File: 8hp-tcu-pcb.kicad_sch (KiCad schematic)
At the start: 0 parts

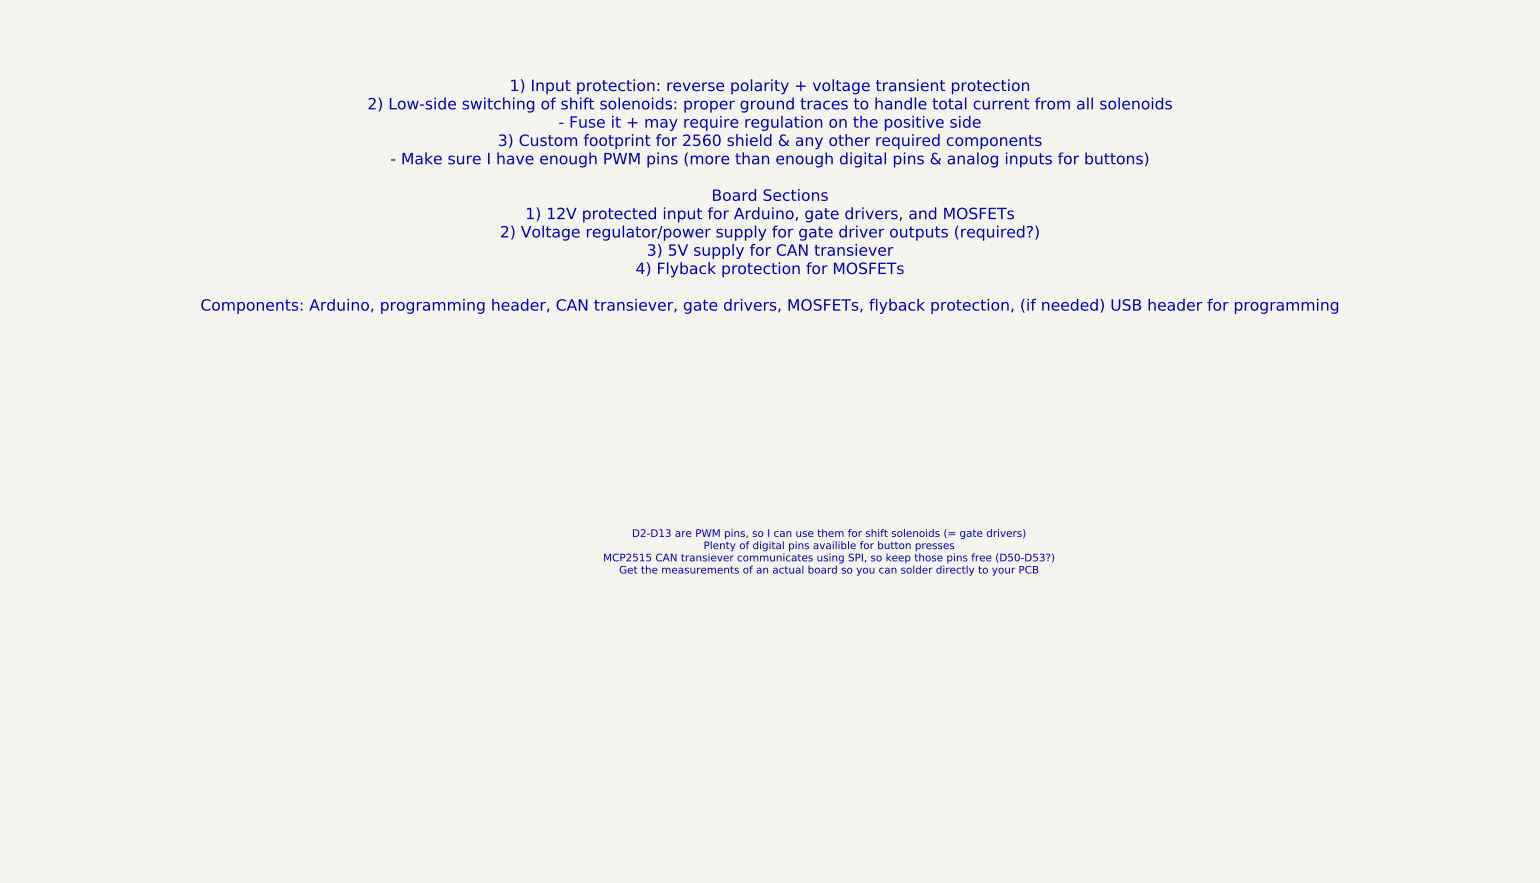
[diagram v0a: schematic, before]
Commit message: Updating several files, made a schematic for internal transmission PCB
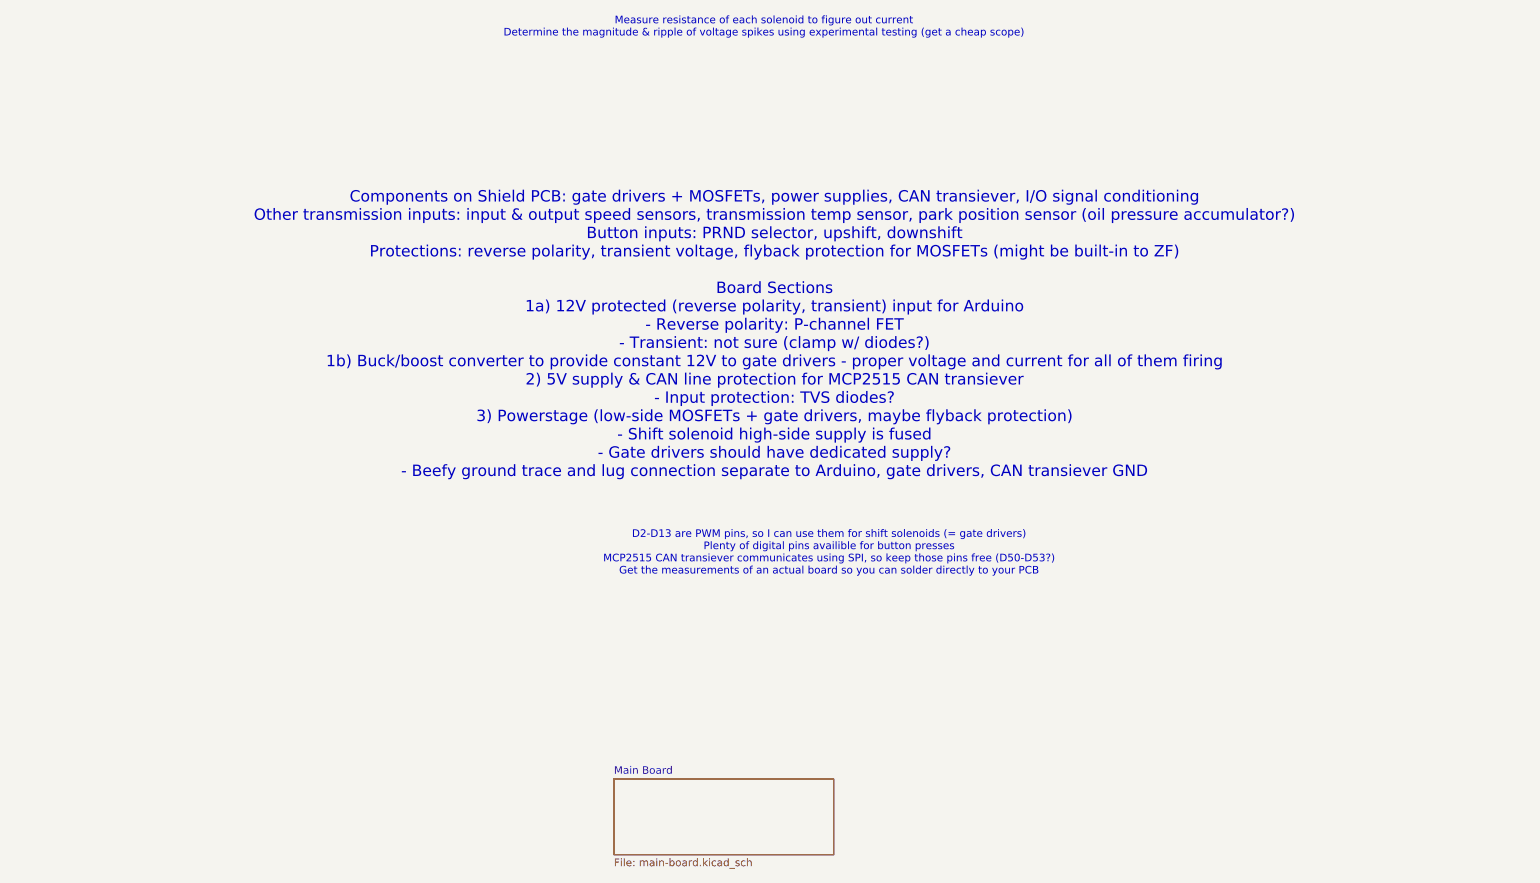
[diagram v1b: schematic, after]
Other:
- added sheet Main Board (main-board.kicad_sch)
- note added: "Components on Shield PCB: gate drivers + MOSFETs, power supplies, CAN transiever, I/O signal conditioning Other transmission inputs: input & output speed sensors, transmission temp sensor, park position sensor (oil pressure accumulator?) Button inputs: PRND selector, upshift, downshift Protections: reverse polarity, transient voltage, flyback protection for MOSFETs (might be built-in to ZF) Board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"
- note added: "Measure resistance of each solenoid to figure out current Determine the magnitude & ripple of voltage spikes using experimental testing (get a cheap scope)"
- note removed: "1) Input protection: reverse polarity + voltage transient protection 2) Low-side switching of shift solenoids: proper ground traces to handle total current from all solenoids - Fuse it + may require regulation on the positive side 3) Custom footprint for 2560 shield & any other required components - Make sure I have enough PWM pins (more than enough digital pins & analog inputs for buttons) Board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"
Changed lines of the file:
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@@
 		(company "Joelathan Racing")
+	)
+	(text "Measure resistance of each solenoid to figure out current\nDetermine the magnitude & ripple of voltage spikes using experimental testing (get a cheap scope)\n"
+		(exclude_from_sim no)
+		(at 125.476 46.736 0)
+		(effects
+			(font
+				(size 1.27 1.27)
+			)
+		)
 	)
 	(text "D2-D13 are PWM pins, so I can use them for shift solenoids (= gate drivers)\nPlenty of digital pins availible for button presses\nMCP2515 CAN transiever communicates using SPI, so keep those pins free (D50-D53?)\nGet the measurements of an actual board so you can solder directly to your PCB"
@@
 		)
 	)
-	(text "1) Input protection: reverse polarity + voltage transient protection\n2) Low-side switching of shift solenoids: proper ground traces to handle total current from all solenoids\n- Fuse it + may require regulation on the positive side\n3) Custom footprint for 2560 shield & any other required components\n- Make sure I have enough PWM pins (more than enough digital pins & analog inputs for buttons)\n\nBoard Sections\n1) 12V protected input for Arduino, gate drivers, and MOSFETs\n2) Voltage regulator/power supply for gate driver outputs (required?)\n3) 5V supply for CAN transiever \n4) Flyback protection for MOSFETs\n\nComponents: Arduino, programming header, CAN transiever, gate drivers, MOSFETs, flyback protection, (if needed) USB header for programming"
+	(text "Components on Shield PCB: gate drivers + MOSFETs, power supplies, CAN transiever, I/O signal conditioning\nOther transmission inputs: input & output speed sensors, transmission temp sensor, park position sensor (oil pressure accumulator?)\nButton inputs: PRND selector, upshift, downshift\nProtections: reverse polarity, transient voltage, flyback protection for MOSFETs (might be built-in to ZF)\n\nBoard Sections\n1a) 12V protected (reverse polarity, transient) input for Arduino\n- Reverse polarity: P-channel FET\n- Transient: not sure (clamp w/ diodes?)\n1b) Buck/boost converter to provide constant 12V to gate drivers - proper voltage and current for all of them firing\n2) 5V supply & CAN line protection for MCP2515 CAN transiever\n- Input protection: TVS diodes?\n3) Powerstage (low-side MOSFETs + gate drivers, maybe flyback protection)\n- Shift solenoid high-side supply is fused\n- Gate drivers should have dedicated supply?\n- Beefy ground trace and lug connection separate to Arduino, gate drivers, CAN transiever GND"
 		(exclude_from_sim no)
-		(at 126.492 75.184 0)
+		(at 127.254 98.298 0)
 		(effects
 			(font
@@
 			)
 		)
+	)
+	(sheet
+		(at 100.33 172.72)
+		(size 36.83 12.7)
+		(fields_autoplaced yes)
+		(stroke
+			(width 0.1524)
+			(type solid)
+		)
+		(fill
+			(color 0 0 0 0.0000)
+		)
+		(property "Sheetname" "Main Board"
+			(at 100.33 172.0084 0)
+			(effects
+				(font
+					(size 1.27 1.27)
+				)
+				(justify left bottom)
+			)
+		)
+		(property "Sheetfile" "main-board.kicad_sch"
+			(at 100.33 186.0046 0)
+			(effects
+				(font
+					(size 1.27 1.27)
+				)
+				(justify left top)
+			)
+		)
+		(instances
+			(project "8hp-tcu-pcb"
+				(path "/fab55a76-018d-479e-806d-47398c1ea91a"
+					(page "2")
+				)
+			)
+		)

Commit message: Repo update
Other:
- sheet Main Board renamed Power Stage
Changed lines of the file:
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@@
 		)
 	)
-	(text "Components on Shield PCB: gate drivers + MOSFETs, power supplies, CAN transiever, I/O signal conditioning\nOther transmission inputs: input & output speed sensors, transmission temp sensor, park position sensor (oil pressure accumulator?)\nButton inputs: PRND selector, upshift, downshift\nProtections: reverse polarity, transient voltage, flyback protection for MOSFETs (might be built-in to ZF)\n\nBoard Sections\n1a) 12V protected (reverse polarity, transient) input for Arduino\n- Reverse polarity: P-channel FET\n- Transient: not sure (clamp w/ diodes?)\n1b) Buck/boost converter to provide constant 12V to gate drivers - proper voltage and current for all of them firing\n2) 5V supply & CAN line protection for MCP2515 CAN transiever\n- Input protection: TVS diodes?\n3) Powerstage (low-side MOSFETs + gate drivers, maybe flyback protection)\n- Shift solenoid high-side supply is fused\n- Gate drivers should have dedicated supply?\n- Beefy ground trace and lug connection separate to Arduino, gate drivers, CAN transiever GND"
+	(text "Components on Shield PCB: gate drivers + MOSFETs, power supplies, CAN transiever, I/O signal conditioning\nOther transmission inputs: input & output speed sensors, transmission temp sensor, park position sensor (oil pressure accumulator?)\nButton inputs: PRND selector, upshift, downshift\nProtections: reverse polarity, transient voltage, flyback protection for MOSFETs (might be built-in to ZF)\n\nBoard Sections\n1a) 12V protected (reverse polarity, transient) input for Arduino\n- Reverse polarity: P-channel FET\n- Transient: not sure (clamp w/ diodes?)\n1b) Buck/boost converter to provide constant 20V to gate drivers - proper voltage and current for all of them firing\n2) 5V supply & CAN line protection for MCP2515 CAN transiever\n- Input protection: TVS diodes?\n3) Powerstage (low-side MOSFETs + gate drivers, and flyback protection)\n- Shift solenoid high-side supply is fused\n- Gate drivers should have dedicated supply?\n- Beefy ground trace and lug connection separate to Arduino, gate drivers, CAN transiever GND"
 		(exclude_from_sim no)
 		(at 127.254 98.298 0)
@@
 			(color 0 0 0 0.0000)
 		)
-		(property "Sheetname" "Main Board"
+		(property "Sheetname" "Power Stage"
 			(at 100.33 172.0084 0)
 			(effects
